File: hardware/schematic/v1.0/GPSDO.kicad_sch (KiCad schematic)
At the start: 59 parts, among them J1 USB_C_Receptacle_USB2.0_16P, Q1 NMOS, SW1 SW_Push, U1 STM32G431KBUx, U2 OCXO-10M, U3 SKG123N, U4 IPEX1, U5 BQ25890, U6 TPS7A8901, U7 CH340E, Y1 Crystal_GND24

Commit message: Update KiCad schematic and project files
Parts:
- added R20, R21: 10K, Resistor_SMD:R_0603_1608Metric, symbol Device:R
- BZ1: footprint (none) -> Counter:BUZ-SMD_L5.0-W5.5-P4.60
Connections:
- net +3.3V: now also R20.2, R21.2
- net I2C1_SCL: now also R21.1
- net I2C1_SDA: now also R20.1
- net OTG: now also U1.26 (PB3)

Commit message: 更新 GPSDO 硬件设计文件
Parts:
- added C22, C23, C24: 100nF, Capacitor_SMD:C_0402_1005Metric, symbol Device:C
- C19, C20: footprint Capacitor_SMD:C_0603_1608Metric -> Capacitor_SMD:C_0402_1005Metric
- R14, R16, R17, R18, R20, R21: footprint Resistor_SMD:R_0603_1608Metric -> Resistor_SMD:R_0402_1005Metric
- SW1: footprint Capacitor_SMD:C_0201_0603Metric -> Button_Switch_SMD:SW_Tactile_SPST_NO_Straight_CK_PTS636Sx25SMTRLFS
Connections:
- net +3.3V: now also C22.1, C23.1, C24.1
- net BAT-: now also C22.2, C23.2, C24.2

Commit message: 更新 GPSDO 硬件原理图和 PCB 文件
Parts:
- removed Q1: NMOS, Button_Switch_SMD:SW_SPST_B3S-1100, symbol Simulation_SPICE:NMOS
- added Q1: AO3400A, Package_TO_SOT_SMD:SOT-23-3, symbol Counter:NMOS_SOT23
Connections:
- net BAT-: now also Q1.2 (S)
- net BUZZ: now also Q1.1 (G)
- net at BZ1.2 (-): now also Q1.3 (D)
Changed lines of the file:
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@@
+	)
+	(symbol
+		(lib_id "Counter:NMOS_SOT23")
+		(at 111.76 181.61 0)
+		(unit 1)
+		(body_style 1)
+		(exclude_from_sim no)
+		(in_bom yes)
+		(on_board yes)
+		(in_pos_files yes)
+		(dnp no)
+		(fields_autoplaced yes)
+		(property "Reference" "Q1"
+			(at 116.84 180.3399 0)
+			(show_name no)
+			(do_not_autoplace no)
+			(effects
+				(font
+					(size 1.27 1.27)
+				)
+				(justify left)
+			)
+		)
+		(property "Value" "AO3400A"
+			(at 116.84 182.8799 0)
+			(show_name no)
+			(do_not_autoplace no)
+			(effects
+				(font
+					(size 1.27 1.27)
+				)
+				(justify left)
+			)
+		)
+		(property "Footprint" "Package_TO_SOT_SMD:SOT-23-3"
+			(at 112.268 171.45 0)
+			(hide yes)
+			(show_name no)
+			(do_not_autoplace no)
+			(effects
+				(font
+					(size 1.27 1.27)
+				)
+			)
+		)
+		(property "Datasheet" ""
+			(at 111.76 181.61 0)
+			(hide yes)
+			(show_name no)
+			(do_not_autoplace no)
+			(effects
+				(font
+					(size 1.27 1.27)
+				)
+			)
+		)
+		(property "Description" ""
+			(at 111.76 181.61 0)
+			(hide yes)
+			(show_name no)
+			(do_not_autoplace no)
+			(effects
+				(font
+					(size 1.27 1.27)
+				)
+			)
+		)
+		(pin "3"
+		)
+		(pin "2"
+		)
+		(pin "1"
+		)
+		(instances
+			(project "GPSDO"
+				(path "/bb9f04d0-06e2-4b9f-871a-754dc45b8574"
+					(reference "Q1")
+					(unit 1)
+				)
+			)
+		)
 	)
 	(symbol
@@
 					(unit 1)
 				)
-			)
-		)
-	)
-	(symbol
-		(lib_id "Simulation_SPICE:NMOS")
-		(at 110.49 181.61 0)
-		(unit 1)
-		(body_style 1)
-		(exclude_from_sim no)
-		(in_bom yes)
-		(on_board yes)
-		(in_pos_files yes)
-		(dnp no)
-		(fields_autoplaced yes)
-		(property "Reference" "Q1"
-			(at 116.84 180.3399 0)
-			(show_name no)
-			(do_not_autoplace no)
-			(effects
-				(font
-					(size 1.27 1.27)
-				)
-				(justify left)
-			)
-		)
-		(property "Value" "NMOS"
-			(at 116.84 182.8799 0)
-			(show_name no)
-			(do_not_autoplace no)
-			(effects
-				(font
-					(size 1.27 1.27)
-				)
-				(justify left)
-			)
-		)
-		(property "Footprint" "Button_Switch_SMD:SW_SPST_B3S-1100"
-			(at 115.57 179.07 0)
-			(hide yes)
-			(show_name no)
-			(do_not_autoplace no)
-			(effects
-				(font
-					(size 1.27 1.27)
-				)
-			)
-		)
-		(property "Datasheet" "https://ngspice.sourceforge.io/docs/ngspice-html-manual/manual.xhtml#cha_MOSFETs"
-			(at 110.49 194.31 0)
-			(hide yes)
-			(show_name no)
-			(do_not_autoplace no)
-			(effects
-				(font
-					(size 1.27 1.27)
-				)
-			)
-		)
-		(property "Description" "N-MOSFET transistor, drain/source/gate"
-			(at 110.49 181.61 0)
-			(hide yes)
-			(show_name no)
-			(do_not_autoplace no)
-			(effects
-				(font
-					(size 1.27 1.27)
-				)
-			)
-		)
-		(property "Sim.Device" "NMOS"
-			(at 110.49 198.755 0)
-			(hide yes)
-			(show_name no)
-			(do_not_autoplace no)
-			(effects
-				(font
-					(size 1.27 1.27)
-				)
-			)
-		)
-		(property "Sim.Type" "VDMOS"
-			(at 110.49 200.66 0)
-			(hide yes)
-			(show_name no)
-			(do_not_autoplace no)
-			(effects
-				(font
-					(size 1.27 1.27)
-				)
-			)
-		)
-		(property "Sim.Pins" "1=D 2=G 3=S"
-			(at 110.49 196.85 0)
-			(hide yes)
-			(show_name no)
-			(do_not_autoplace no)
-			(effects
-				(font
-					(size 1.27 1.27)
-				)
-			)
-		)
-		(pin "2"
-		)
-		(pin "1"
-		)
-		(pin "3"
-		)
-		(instances
-			(project "GPSDO"
-				(path "/bb9f04d0-06e2-4b9f-871a-754dc45b8574"
-					(reference "Q1")
-					(unit 1)
-				)

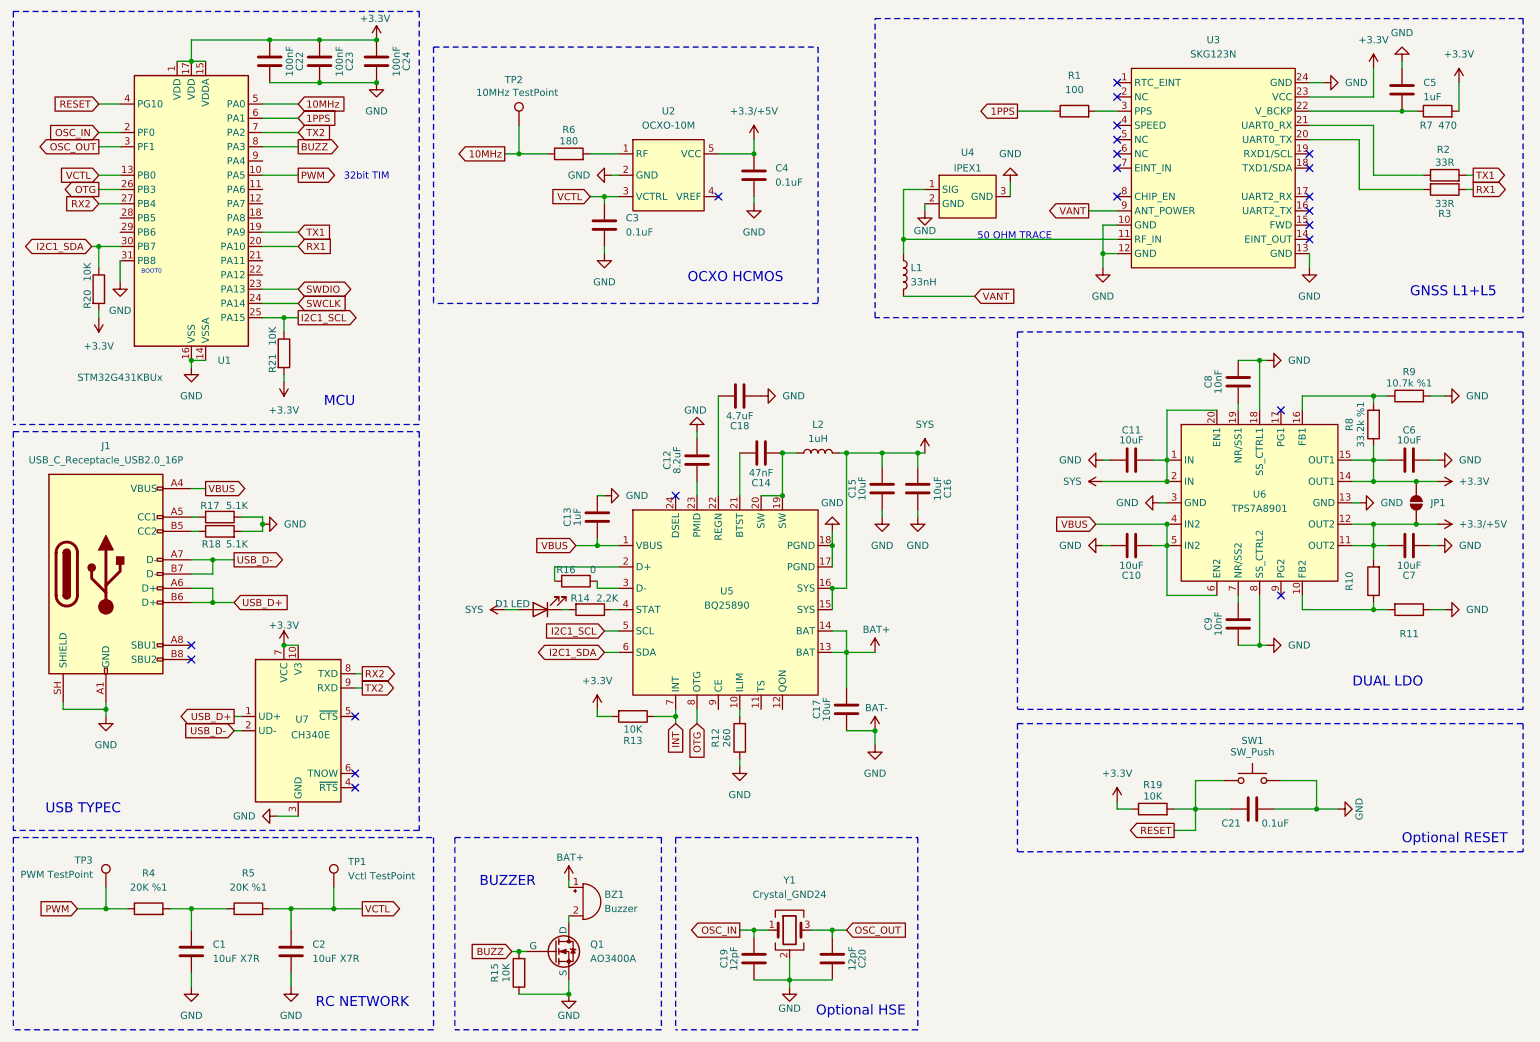
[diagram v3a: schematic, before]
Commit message: 更新 GPSDO 硬件原理图和 PCB 设计文件
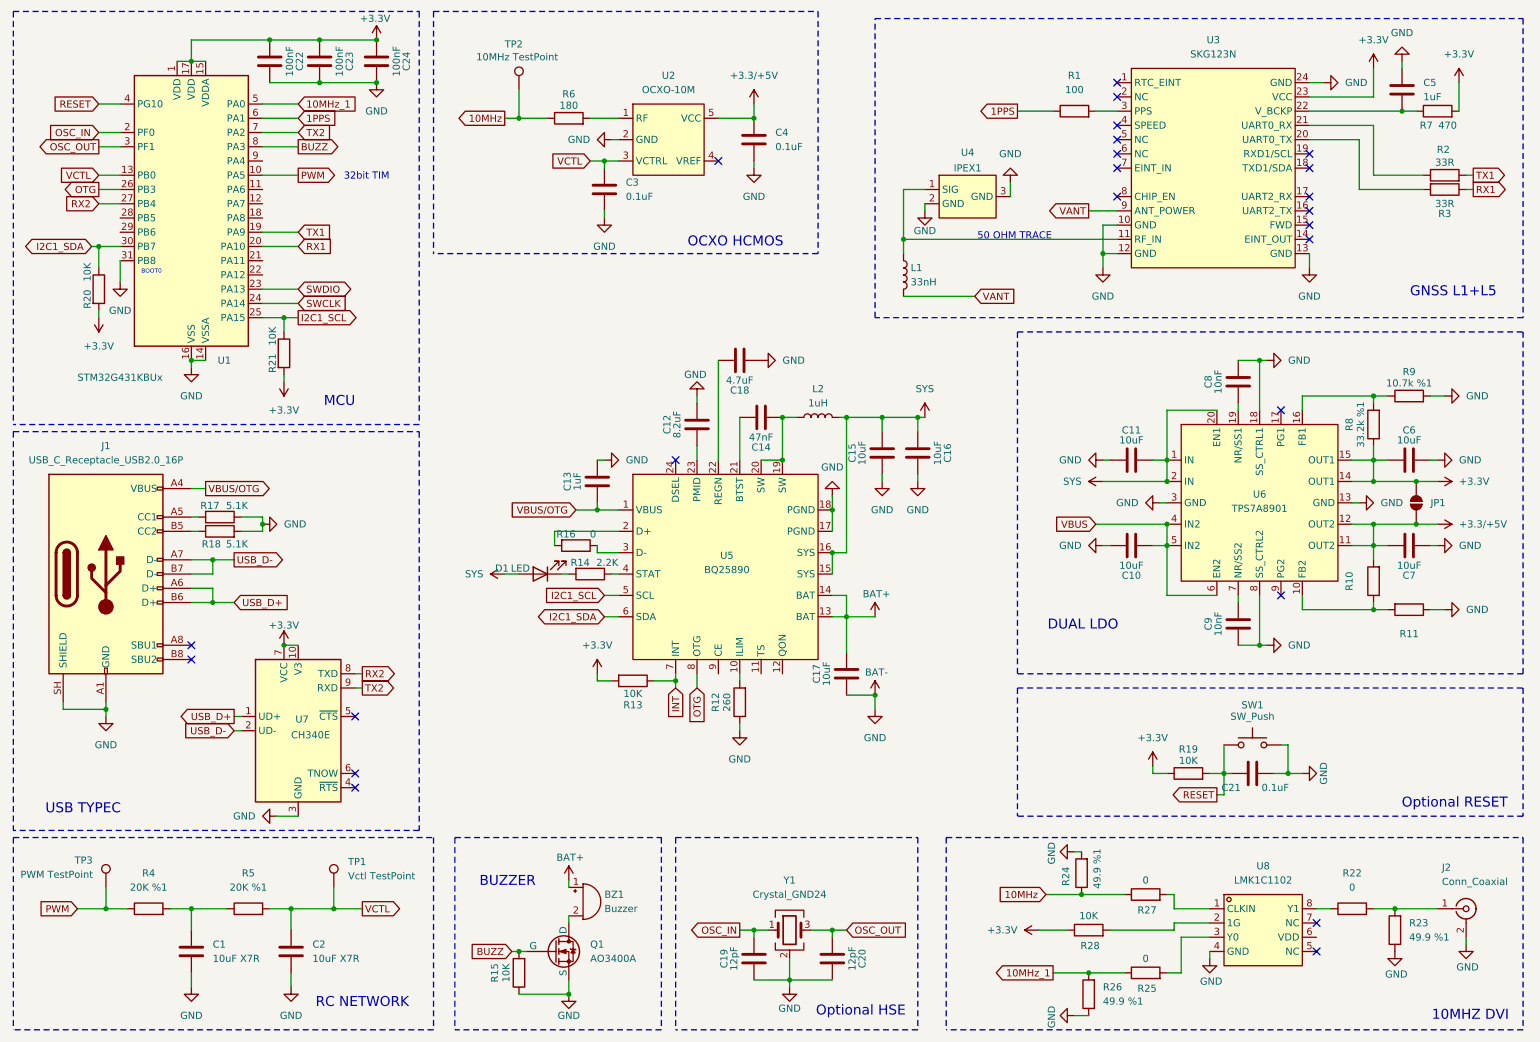
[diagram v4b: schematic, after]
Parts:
- added J2: Conn_Coaxial, Connector_Coaxial:SMA_Amphenol_132289_EdgeMount, symbol Connector:Conn_Coaxial
- added R22, R25, R27: 0, Resistor_SMD:R_0402_1005Metric, symbol Device:R
- added R23, R24, R26: 49.9 %1, Resistor_SMD:R_0402_1005Metric, symbol Device:R
- added R28: 10K, Resistor_SMD:R_0402_1005Metric, symbol Device:R
- added U8: LMK1C1102, Package_SON:WSON-8-1EP_2x2mm_P0.5mm_EP0.9x1.6mm, symbol Counter:LMK1C1102
- C21: footprint Capacitor_SMD:C_0603_1608Metric -> Capacitor_SMD:C_0402_1005Metric
- R19: footprint Resistor_SMD:R_0603_1608Metric -> Resistor_SMD:R_0402_1005Metric
- SW1: footprint Button_Switch_SMD:SW_Tactile_SPST_NO_Straight_CK_PTS636Sx25SMTRLFS -> Counter:KEY-SMD_B3U-1000PM
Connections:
- net +3.3V: now also R28.1
- net 10MHz: now also R24.1, R27.1; no longer U1.5 (PA0)
- net BAT-: now also J2.2 (Ext), R23.1, R24.2, R26.1, U8.4 (GND)
- net VBUS: no longer C13.1, J1.A4 (VBUS), J1.A9 (VBUS), J1.B4 (VBUS), J1.B9 (VBUS), U5.1 (VBUS)
- new net: R22.1, U8.8 (Y1)
- new net: J2.1 (In), R22.2, R23.2
- new net: R27.2, U8.1 (CLKIN)
- new net: R28.2, U8.2 (1G)
- new net: R25.2, U8.3 (Y0)
- new net 10MHz_1: R25.1, R26.2, U1.5 (PA0)
- new net VBUS/OTG: C13.1, J1.A4 (VBUS), J1.A9 (VBUS), J1.B4 (VBUS), J1.B9 (VBUS), U5.1 (VBUS)
- no-connect marks 22 -> 24
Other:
- note added: "10MHZ DVI"
- moved on the sheet: C12, C13, C14, C15, C16, C17, C18, C21, C3, C4, D1, L2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

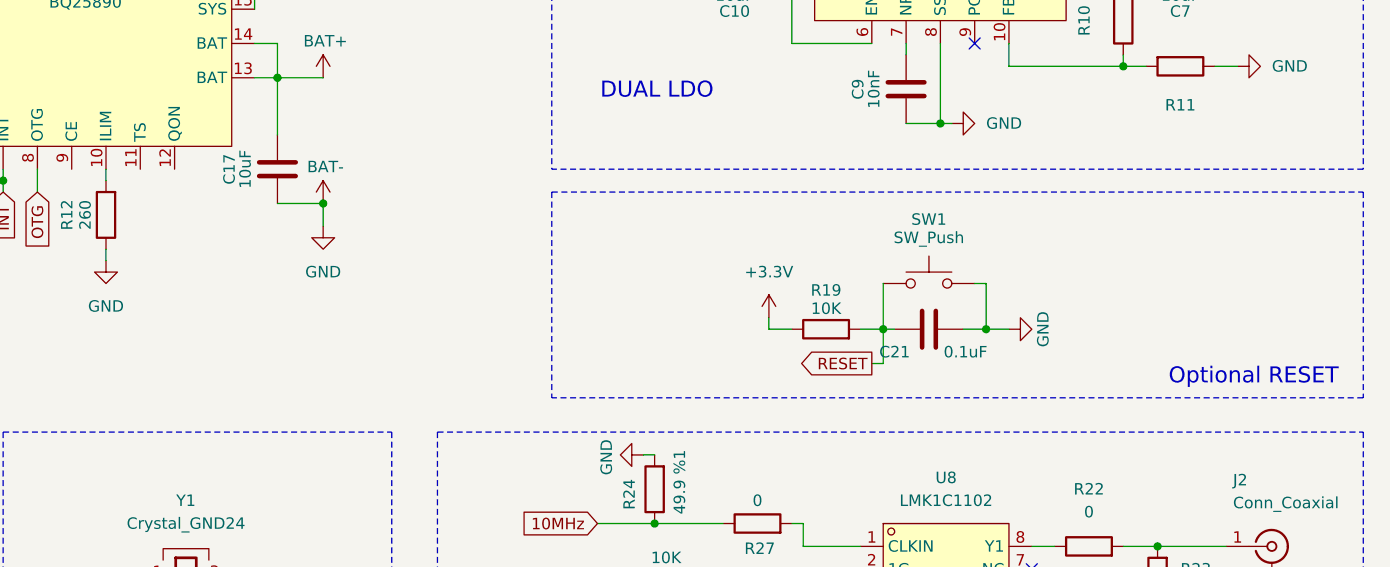
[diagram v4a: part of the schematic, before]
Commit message: 更新原理图与PCB设计
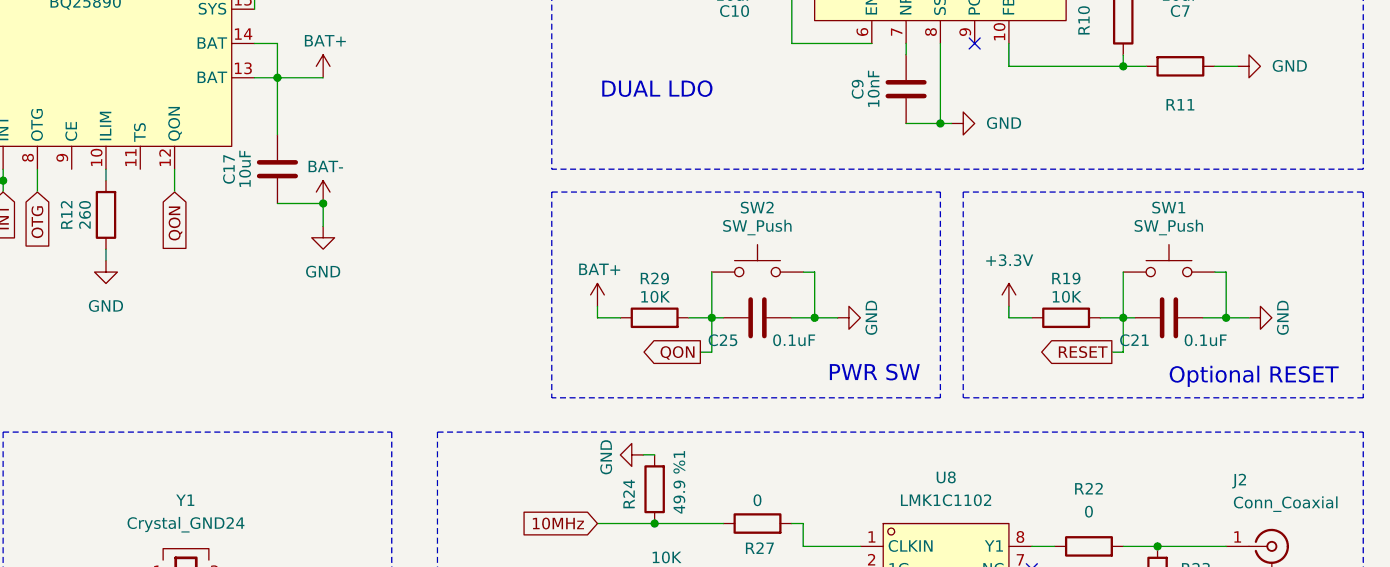
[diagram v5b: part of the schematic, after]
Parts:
- added C25: 0.1uF, Capacitor_SMD:C_0402_1005Metric, symbol Device:C
- added R29: 10K, Resistor_SMD:R_0402_1005Metric, symbol Device:R
- added SW2: SW_Push, Counter:KEY-SMD_B3U-1000PM, symbol Switch:SW_Push
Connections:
- net BAT+: now also R29.1
- net BAT-: now also C25.1, SW2.2
- net QON: now reaches U5.12 (QON)
- net QON: now also C25.2, R29.2, SW2.1
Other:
- note added: "PWR SW"
- moved on the sheet: C21, R19, SW1

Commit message: sch update
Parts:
- added C26: 10uF, Capacitor_SMD:C_0402_1005Metric, symbol Device:C
- added C27: 100nF, Capacitor_SMD:C_0402_1005Metric, symbol Device:C
- U4: footprint (none) -> Counter:JLC_IPEX-1
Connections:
- net +3.3V: now also U8.6 (VDD), C26.1, C27.1
- net BAT-: now also U4.1 (GND), C26.2, C27.2
- net at L1.1, U3.11 (RF_IN): now also U4.4 (SIG); no longer U4.1 (SIG)
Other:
- moved on the sheet: L1

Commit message: sch update
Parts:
- added FB1: 100R@100MHz/2A, Inductor_SMD:L_1206_3216Metric, symbol Device:FerriteBead_Small
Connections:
- net +3.3/+5V: now also FB1.1; no longer C4.1, U2.5 (VCC)
- new net: C4.1, FB1.2, U2.5 (VCC)
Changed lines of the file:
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@@
 	(polyline
 		(pts
-			(xy 157.48 13.97) (xy 157.48 57.15)
+			(xy 161.29 13.97) (xy 161.29 57.15)
 		)
 		(stroke
@@
 	(wire
 		(pts
+			(xy 146.05 31.75) (xy 146.05 33.02)
+		)
+		(stroke
+			(width 0)
+			(type default)
+		)
+	)
+	(wire
+		(pts
 			(xy 71.12 170.18) (xy 71.12 173.99)
 		)
@@
 	(polyline
 		(pts
-			(xy 157.48 57.15) (xy 88.9 57.15)
+			(xy 161.29 57.15) (xy 88.9 57.15)
 		)
 		(stroke
@@
 	(wire
 		(pts
-			(xy 146.05 30.48) (xy 146.05 33.02)
+			(xy 146.05 24.13) (xy 146.05 26.67)
 		)
 		(stroke
@@
 	(polyline
 		(pts
-			(xy 88.9 13.97) (xy 157.48 13.97)
+			(xy 88.9 13.97) (xy 161.29 13.97)
 		)
 		(stroke
@@
 	(symbol
 		(lib_id "power:+3.3V")
-		(at 146.05 30.48 0)
+		(at 146.05 24.13 0)
 		(unit 1)
 		(body_style 1)
@@
 		(fields_autoplaced yes)
 		(property "Reference" "#PWR028"
-			(at 146.05 34.29 0)
+			(at 146.05 27.94 0)
 			(hide yes)
 			(show_name no)
@@
 		)
 		(property "Value" "+3.3/+5V"
-			(at 146.05 25.4 0)
+			(at 146.05 19.05 0)
 			(show_name no)
 			(do_not_autoplace no)
@@
 		)
 		(property "Footprint" ""
-			(at 146.05 30.48 0)
+			(at 146.05 24.13 0)
 			(hide yes)
 			(show_name no)
@@
 		)
 		(property "Datasheet" ""
-			(at 146.05 30.48 0)
+			(at 146.05 24.13 0)
 			(hide yes)
 			(show_name no)
@@
 		)
 		(property "Description" "Power symbol creates a global label with name \"+3.3V\""
-			(at 146.05 30.48 0)
+			(at 146.05 24.13 0)
 			(hide yes)
 			(show_name no)
@@
 					(unit 1)
 				)
+			)
+		)
+	)
+	(symbol
+		(lib_id "Device:FerriteBead_Small")
+		(at 146.05 29.21 0)
+		(unit 1)
+		(body_style 1)
+		(exclude_from_sim no)
+		(in_bom yes)
+		(on_board yes)
+		(in_pos_files yes)
+		(dnp no)
+		(property "Reference" "FB1"
+			(at 141.732 24.892 0)
+			(show_name no)
+			(do_not_autoplace no)
+			(effects
+				(font
+					(size 1.27 1.27)
+				)
+				(justify left)
+			)
+		)
+		(property "Value" "100R@100MHz/2A"
+			(at 146.304 26.924 0)
+			(show_name no)
+			(do_not_autoplace no)
+			(effects
+				(font
+					(size 1.27 1.27)
+				)
+				(justify left)
+			)
+		)
+		(property "Footprint" "Inductor_SMD:L_1206_3216Metric"
+			(at 144.272 29.21 90)
+			(hide yes)
+			(show_name no)
+			(do_not_autoplace no)
+			(effects
+				(font
+					(size 1.27 1.27)
+				)
+			)
+		)
+		(property "Datasheet" ""
+			(at 146.05 29.21 0)
+			(hide yes)
+			(show_name no)
+			(do_not_autoplace no)
+			(effects
+				(font
+					(size 1.27 1.27)
+				)
+			)
+		)
+		(property "Description" "OCXO VCC 滤波磁珠，DCR 不大于 0.02 欧，额定电流不小于 2 A"
+			(at 146.05 29.21 0)
+			(hide yes)
+			(show_name no)
+			(do_not_autoplace no)
+			(effects
+				(font
+					(size 1.27 1.27)
+				)
+			)
+		)
+		(pin "1"
+		)
+		(pin "2"
+		)
+		(instances
+			(project "GPSDO"
+				(path "/bb9f04d0-06e2-4b9f-871a-754dc45b8574"
+					(reference "FB1")
+					(unit 1)
+				)
